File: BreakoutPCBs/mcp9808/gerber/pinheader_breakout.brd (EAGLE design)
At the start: 25.4 x 25.4 mm, 4 parts

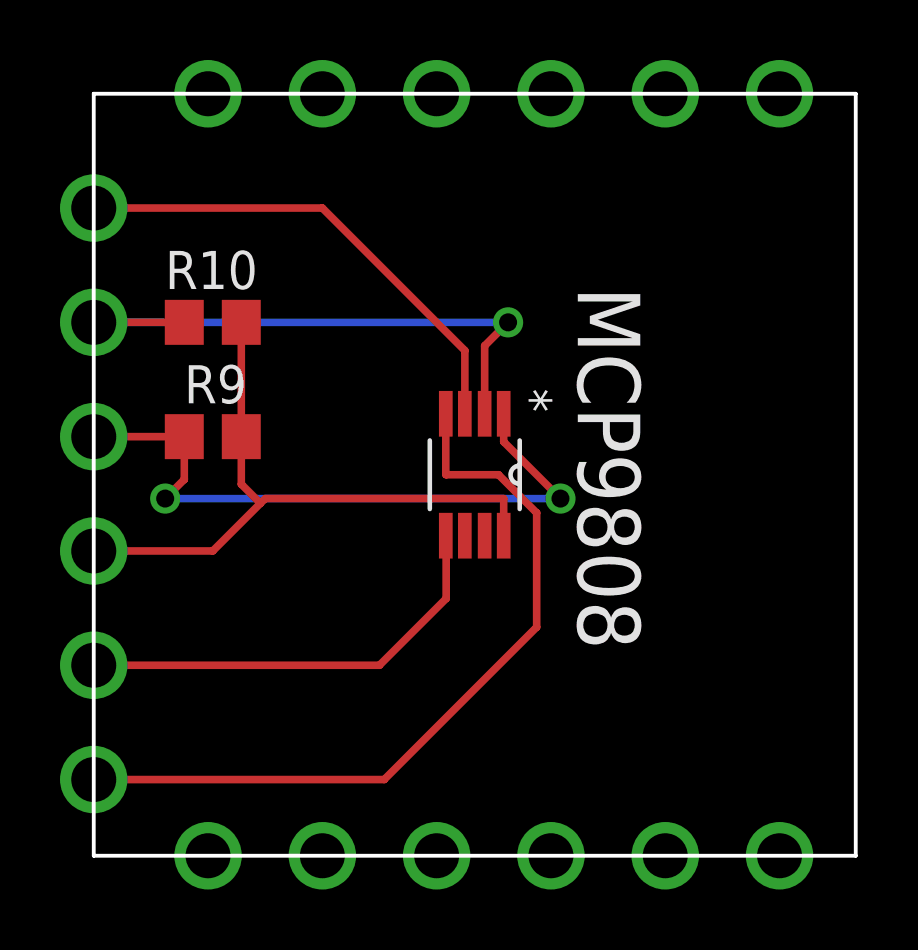
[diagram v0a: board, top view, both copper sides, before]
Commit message: update mcp breakout
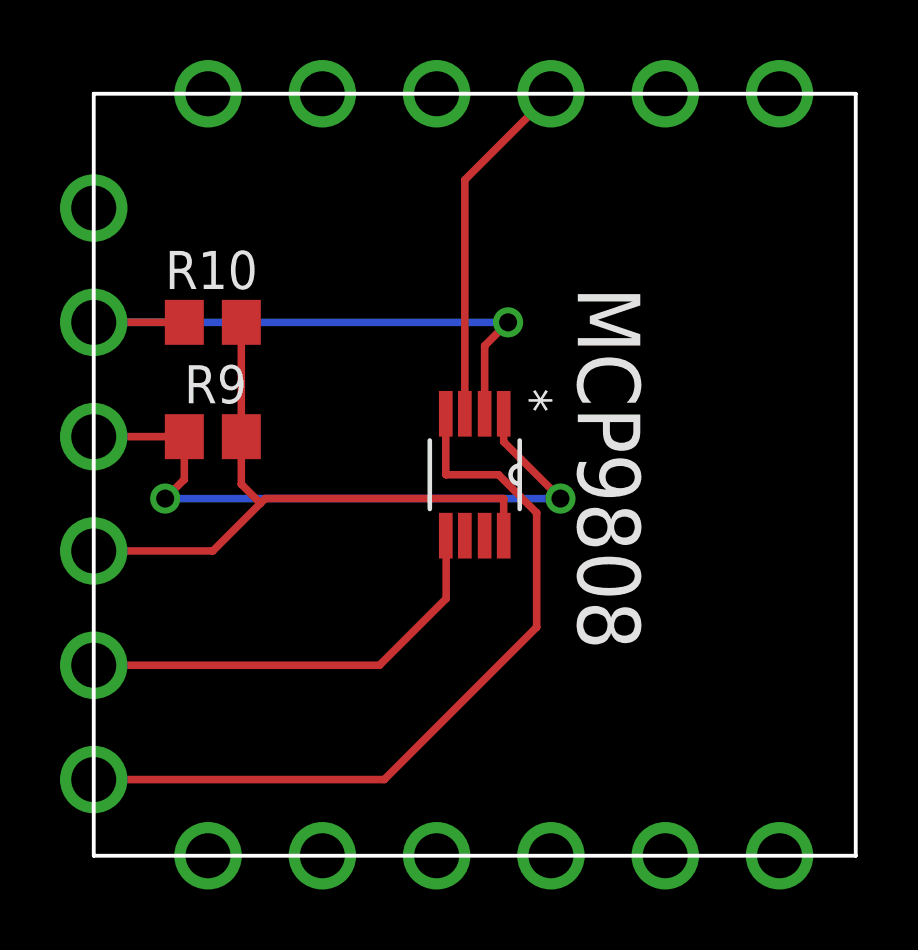
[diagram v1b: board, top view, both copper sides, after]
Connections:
- removed net PB2: U$1.P$9
- new net MOSI: U$1.P$13
- net ALERT: now also U$1.P$9; no longer U$1.P$13
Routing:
- net ALERT: track 16.4 -> 11.9 mm
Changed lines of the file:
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@@
 <contactref element="U$1" pad="P$12"/>
+</signal>
+<signal name="MOSI">
+<contactref element="U$1" pad="P$13"/>
 </signal>
 <signal name="PA4">
@@
 <signal name="ALERT">
 <contactref element="MCP9808" pad="3"/>
-<contactref element="U$1" pad="P$13"/>
-<wire x1="12.3698" y1="14.732" x2="12.3698" y2="16.8402" width="0.254" layer="1"/>
-<wire x1="12.3698" y1="16.8402" x2="7.62" y2="21.59" width="0.254" layer="1"/>
-<wire x1="7.62" y1="21.59" x2="0" y2="21.59" width="0.254" layer="1"/>
-</signal>
-<signal name="PB2">
 <contactref element="U$1" pad="P$9"/>
+<wire x1="12.3698" y1="14.732" x2="12.3698" y2="22.5298" width="0.254" layer="1"/>
+<wire x1="12.3698" y1="22.5298" x2="15.24" y2="25.4" width="0.254" layer="1"/>
 </signal>
 </signals>
